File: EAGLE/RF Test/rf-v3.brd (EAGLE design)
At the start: 20.3 x 35.6 mm, 9 parts, among them X1 SMA-142-0701-881/886, X2 IPEX-20279-001E

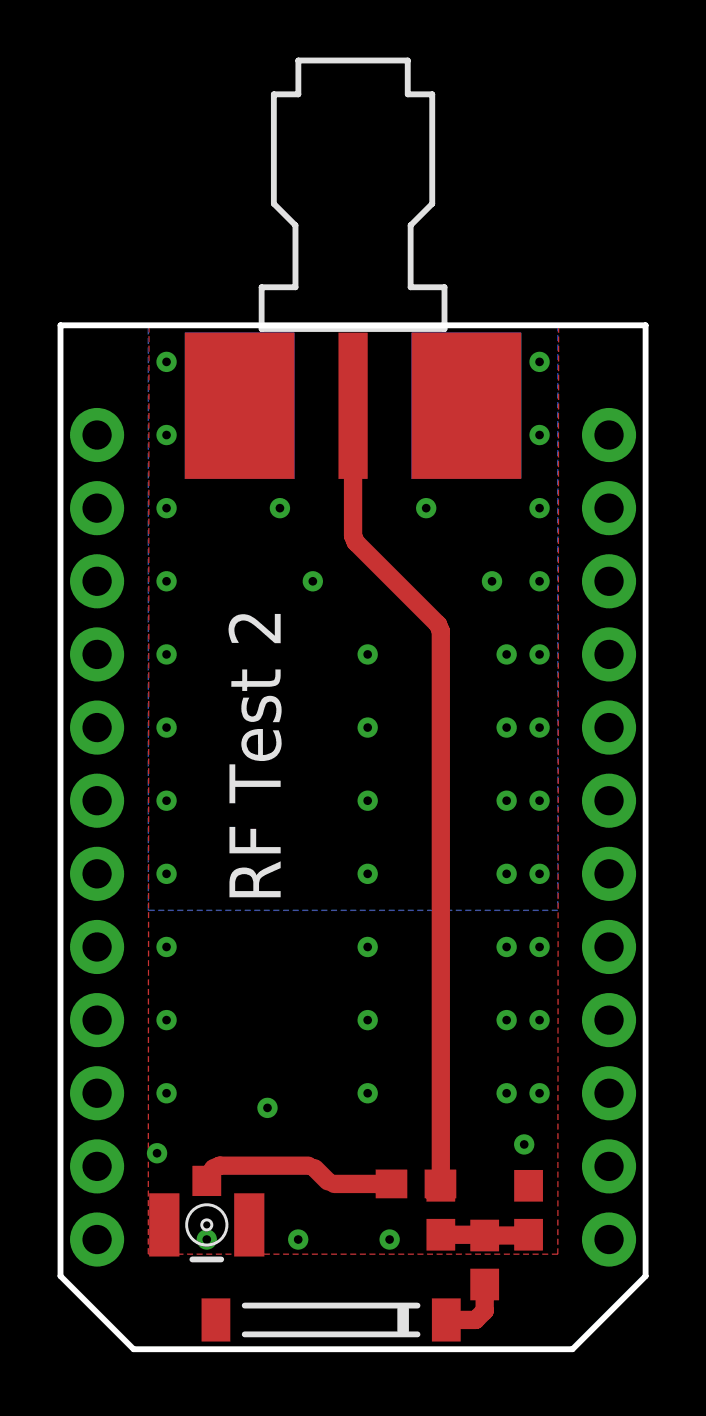
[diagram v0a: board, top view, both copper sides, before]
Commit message: Added RF test boards and their gerbers
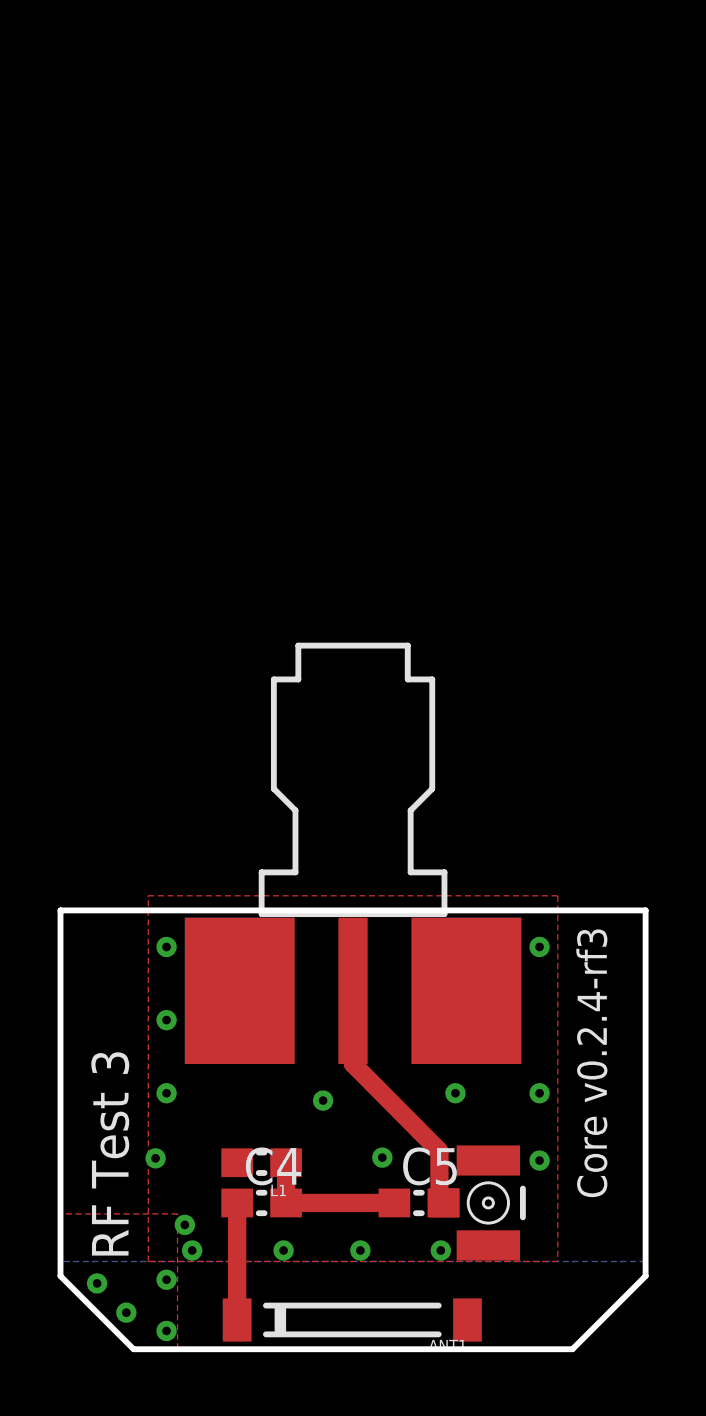
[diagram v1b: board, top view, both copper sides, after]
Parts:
- removed C12, C16: 10pF, rcl:C0603
- removed JP1, JP2: (no value), SparkFun:1X12
- added C5: 10pF, rcl:C0603
- moved X1 20.3 mm to (10.2, 12.5)
- moved X2 9.81 mm to (14.9, 2.54), turned to 90 degrees
- moved L1 9.42 mm to (6.99, 3.94), turned to 180 degrees
- moved C4 8.00 mm to (6.99, 2.54), turned to 0 degrees
- moved ANT1 0.74 mm to (10.1, -1.52), turned to 180 degrees
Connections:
- removed net !RST: JP2.2
- removed net +3V3: JP2.1
- removed net A0: JP1.12
- removed net A1: JP1.11
- removed net A2: JP1.10
- removed net A3: JP1.9
- removed net A4: JP1.8
- removed net A5: JP1.7
- removed net A6: JP1.6
- removed net A7: JP1.5
- removed net D0: JP2.12
- removed net D1: JP2.11
- removed net D2: JP2.10
- removed net D3: JP2.9
- removed net D4: JP2.8
- removed net D5: JP2.7
- removed net D6: JP2.6
- removed net D7: JP2.5
- removed net N$5: C12.1, C4.2, L1.1
- removed net RAW: JP1.1
- removed net RX: JP1.4
- removed net TX: JP1.3
- removed net VDDA: JP2.3
- new net N$1: C4.2, C5.1, L1.1
- net GND: no longer JP1.2, JP2.4
- net N$2: now also C5.2; no longer C16.2
- net N$4: no longer C12.2, C16.1
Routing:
- net N$4: track 28.4 -> 2.29 mm
- net N$2: track 6.96 -> 1.79 mm
- net N$1: track 0.00 -> 5.16 mm
- net S$1: track 0.00 -> 4.38 mm
- net N$5: track 3.07 -> 0.00 mm
- net N$3: track 2.38 -> 4.06 mm
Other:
- board size 20.3 x 35.6 mm -> 20.3 x 15.2 mm
- board text added: "Core v0.2.4-rf3"
- board text added: "RF Test 3"
- board text removed: "RF Test 2"
